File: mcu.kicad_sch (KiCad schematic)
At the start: 7 parts, among them U7 RP2040

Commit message: simulation
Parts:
- C12, C14, C15, C16, C17, C5: value C -> 10n; Part Number (none) -> -
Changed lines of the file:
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@@
 			)
 		)
-		(property "Value" "C"
+		(property "Value" "10n"
 			(at 166.37 30.4799 0)
 			(effects
@@
 				)
 				(hide yes)
+			)
+		)
+		(property "Part Number" "-"
+			(at 162.56 29.21 0)
+			(effects
+				(font
+					(size 1.27 1.27)
+				)
 			)
 		)
@@
 			)
 		)
+		(property "Part Number" ""
+			(at 127 81.28 0)
+			(effects
+				(font
+					(size 1.27 1.27)
+				)
+			)
+		)
 		(pin "55"
 		)
@@
 			)
 		)
-		(property "Value" "C"
+		(property "Value" "10n"
 			(at 106.68 30.4799 0)
 			(effects
@@
 				)
 				(hide yes)
+			)
+		)
+		(property "Part Number" "-"
+			(at 102.87 29.21 0)
+			(effects
+				(font
+					(size 1.27 1.27)
+				)
 			)
 		)
@@
 			)
 		)
-		(property "Value" "C"
+		(property "Value" "10n"
 			(at 146.05 30.4799 0)
 			(effects
@@
 				)
 				(hide yes)
+			)
+		)
+		(property "Part Number" "-"
+			(at 142.24 29.21 0)
+			(effects
+				(font
+					(size 1.27 1.27)
+				)
 			)
 		)
@@
 			)
 		)
-		(property "Value" "C"
+		(property "Value" "10n"
 			(at 116.84 30.4799 0)
 			(effects
@@
 				)
 				(hide yes)
+			)
+		)
+		(property "Part Number" "-"
+			(at 113.03 29.21 0)
+			(effects
+				(font
+					(size 1.27 1.27)
+				)
 			)
 		)
@@
 			)
 		)
-		(property "Value" "C"
+		(property "Value" "10n"
 			(at 156.21 30.4799 0)
 			(effects
@@
 				)
 				(hide yes)
+			)
+		)
+		(property "Part Number" "-"
+			(at 152.4 29.21 0)
+			(effects
+				(font
+					(size 1.27 1.27)
+				)
 			)
 		)
@@
 			)
 		)
-		(property "Value" "C"
+		(property "Value" "10n"
 			(at 96.52 30.4799 0)
 			(effects
@@
 			)
 		)
+		(property "Part Number" "-"
+			(at 92.71 29.21 0)
+			(effects
+				(font
+					(size 1.27 1.27)
+				)
+			)
+		)

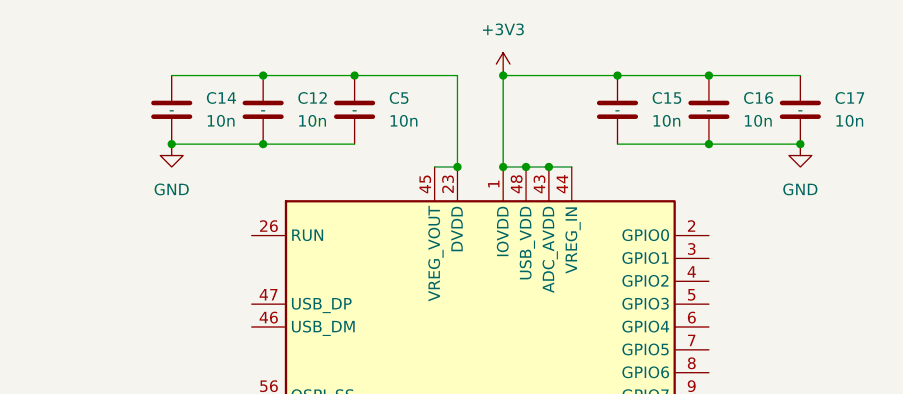
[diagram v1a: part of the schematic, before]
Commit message: new FET
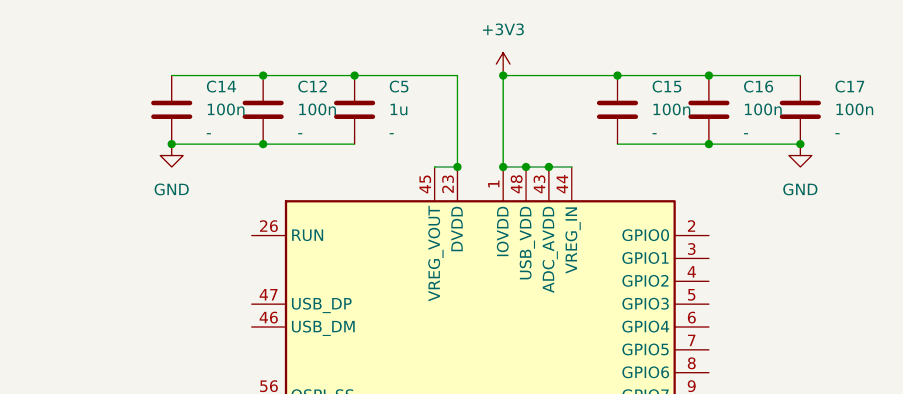
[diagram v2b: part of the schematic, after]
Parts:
- C12, C14, C15, C16, C17: value 10n -> 100n
- C5: value 10n -> 1u
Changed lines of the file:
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@@
 		(fields_autoplaced yes)
 		(property "Reference" "C17"
-			(at 166.37 27.9399 0)
-			(effects
-				(font
-					(size 1.27 1.27)
-				)
-				(justify left)
-			)
-		)
-		(property "Value" "10n"
-			(at 166.37 30.4799 0)
+			(at 166.37 26.6699 0)
+			(effects
+				(font
+					(size 1.27 1.27)
+				)
+				(justify left)
+			)
+		)
+		(property "Value" "100n"
+			(at 166.37 29.2099 0)
 			(effects
 				(font
@@
 		)
 		(property "Part Number" "-"
-			(at 162.56 29.21 0)
-			(effects
-				(font
-					(size 1.27 1.27)
-				)
+			(at 166.37 31.7499 0)
+			(effects
+				(font
+					(size 1.27 1.27)
+				)
+				(justify left)
 			)
 		)
@@
 		(fields_autoplaced yes)
 		(property "Reference" "C12"
-			(at 106.68 27.9399 0)
-			(effects
-				(font
-					(size 1.27 1.27)
-				)
-				(justify left)
-			)
-		)
-		(property "Value" "10n"
-			(at 106.68 30.4799 0)
+			(at 106.68 26.6699 0)
+			(effects
+				(font
+					(size 1.27 1.27)
+				)
+				(justify left)
+			)
+		)
+		(property "Value" "100n"
+			(at 106.68 29.2099 0)
 			(effects
 				(font
@@
 		)
 		(property "Part Number" "-"
-			(at 102.87 29.21 0)
-			(effects
-				(font
-					(size 1.27 1.27)
-				)
+			(at 106.68 31.7499 0)
+			(effects
+				(font
+					(size 1.27 1.27)
+				)
+				(justify left)
 			)
 		)
@@
 		(fields_autoplaced yes)
 		(property "Reference" "C15"
-			(at 146.05 27.9399 0)
-			(effects
-				(font
-					(size 1.27 1.27)
-				)
-				(justify left)
-			)
-		)
-		(property "Value" "10n"
-			(at 146.05 30.4799 0)
+			(at 146.05 26.6699 0)
+			(effects
+				(font
+					(size 1.27 1.27)
+				)
+				(justify left)
+			)
+		)
+		(property "Value" "100n"
+			(at 146.05 29.2099 0)
 			(effects
 				(font
@@
 		)
 		(property "Part Number" "-"
-			(at 142.24 29.21 0)
-			(effects
-				(font
-					(size 1.27 1.27)
-				)
+			(at 146.05 31.7499 0)
+			(effects
+				(font
+					(size 1.27 1.27)
+				)
+				(justify left)
 			)
 		)
@@
 		(fields_autoplaced yes)
 		(property "Reference" "C5"
-			(at 116.84 27.9399 0)
-			(effects
-				(font
-					(size 1.27 1.27)
-				)
-				(justify left)
-			)
-		)
-		(property "Value" "10n"
-			(at 116.84 30.4799 0)
+			(at 116.84 26.6699 0)
+			(effects
+				(font
+					(size 1.27 1.27)
+				)
+				(justify left)
+			)
+		)
+		(property "Value" "1u"
+			(at 116.84 29.2099 0)
 			(effects
 				(font
@@
 		)
 		(property "Part Number" "-"
-			(at 113.03 29.21 0)
-			(effects
-				(font
-					(size 1.27 1.27)
-				)
+			(at 116.84 31.7499 0)
+			(effects
+				(font
+					(size 1.27 1.27)
+				)
+				(justify left)
 			)
 		)
@@
 		(fields_autoplaced yes)
 		(property "Reference" "C16"
-			(at 156.21 27.9399 0)
-			(effects
-				(font
-					(size 1.27 1.27)
-				)
-				(justify left)
-			)
-		)
-		(property "Value" "10n"
-			(at 156.21 30.4799 0)
+			(at 156.21 26.6699 0)
+			(effects
+				(font
+					(size 1.27 1.27)
+				)
+				(justify left)
+			)
+		)
+		(property "Value" "100n"
+			(at 156.21 29.2099 0)
 			(effects
 				(font
@@
 		)
 		(property "Part Number" "-"
-			(at 152.4 29.21 0)
-			(effects
-				(font
-					(size 1.27 1.27)
-				)
+			(at 156.21 31.7499 0)
+			(effects
+				(font
+					(size 1.27 1.27)
+				)
+				(justify left)
 			)
 		)
@@
 		(fields_autoplaced yes)
 		(property "Reference" "C14"
-			(at 96.52 27.9399 0)
-			(effects
-				(font
-					(size 1.27 1.27)
-				)
-				(justify left)
-			)
-		)
-		(property "Value" "10n"
-			(at 96.52 30.4799 0)
+			(at 96.52 26.6699 0)
+			(effects
+				(font
+					(size 1.27 1.27)
+				)
+				(justify left)
+			)
+		)
+		(property "Value" "100n"
+			(at 96.52 29.2099 0)
 			(effects
 				(font
@@
 		)
 		(property "Part Number" "-"
-			(at 92.71 29.21 0)
-			(effects
-				(font
-					(size 1.27 1.27)
-				)
-			)
-		)
+			(at 96.52 31.7499 0)
+			(effects
+				(font
+					(size 1.27 1.27)
+				)
+				(justify left)
+			)
+		)

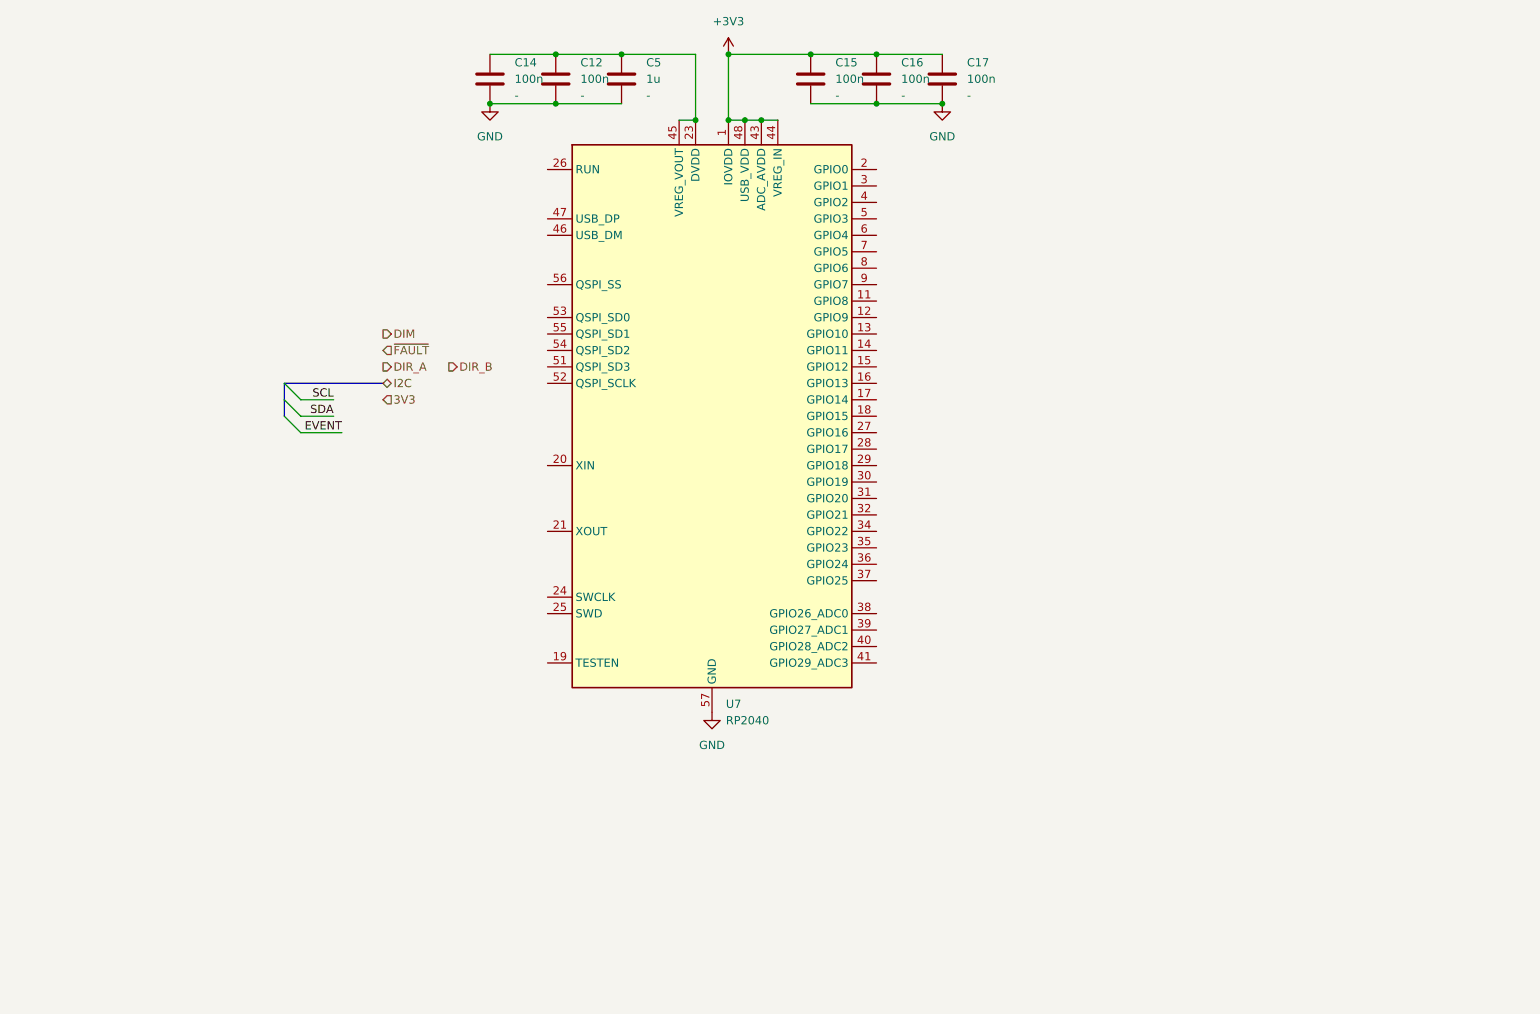
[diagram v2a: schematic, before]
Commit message: updated components
New ganfet selected and further work developing the rp2040 microcontroller circuit
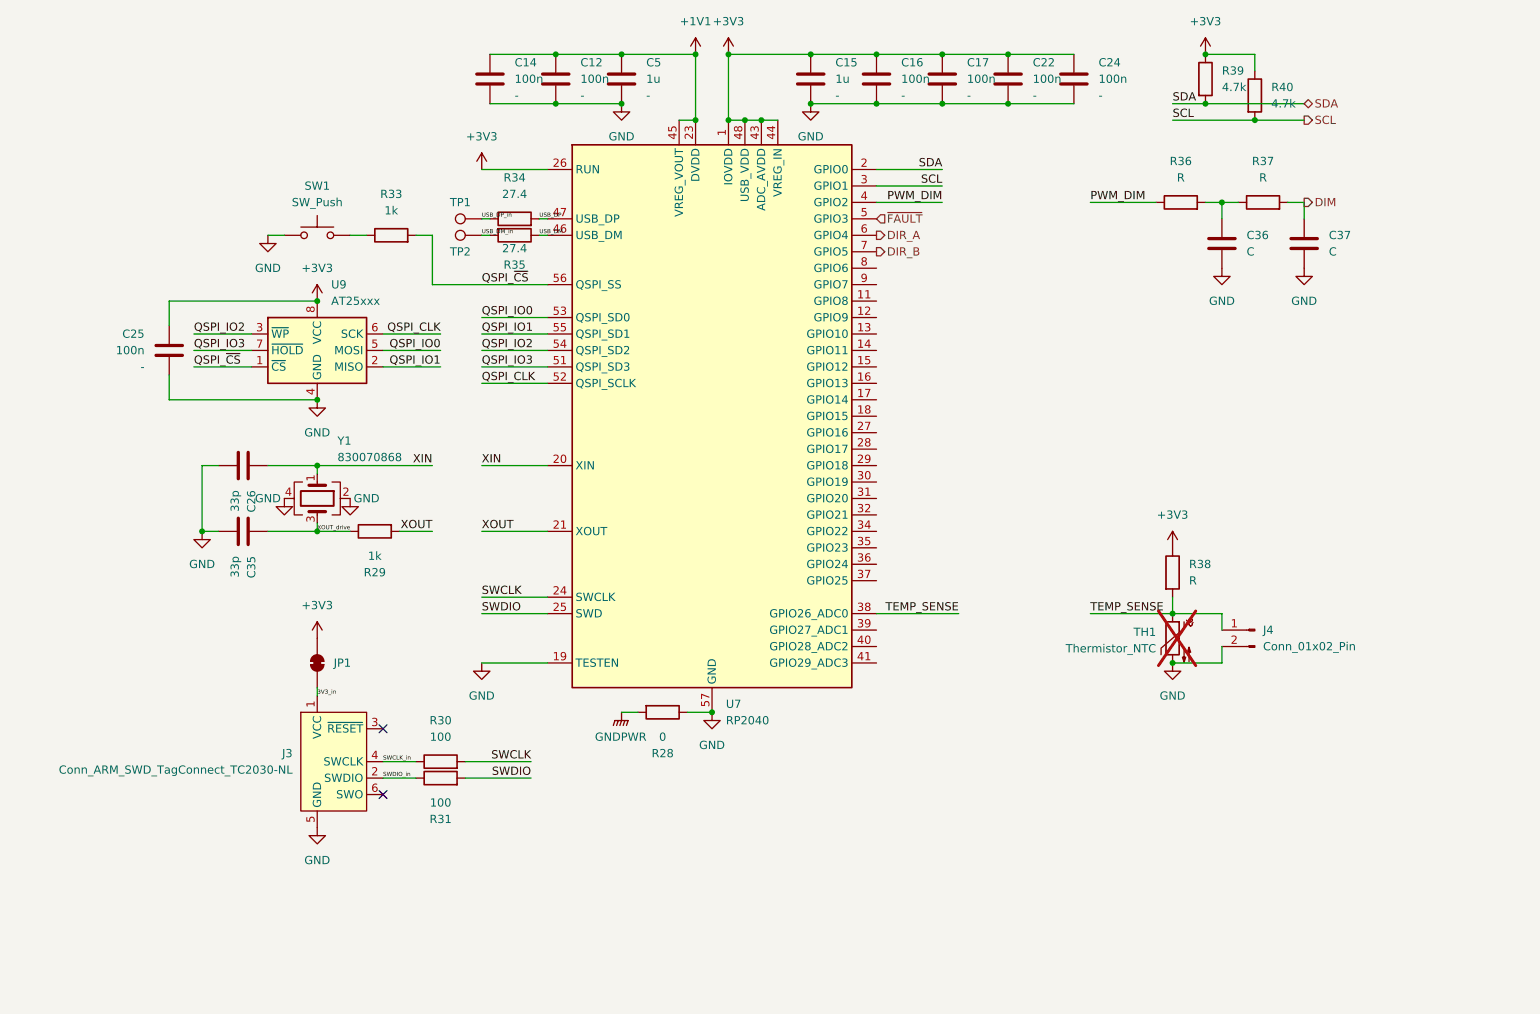
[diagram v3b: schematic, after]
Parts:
- added C22, C24, C25: 100n, Capacitor_SMD:C_0603_1608Metric, symbol Device:C
- added C26, C35: 33p, Capacitor_SMD:C_0603_1608Metric, symbol Device:C
- added C36, C37: C, Capacitor_SMD:C_0603_1608Metric, symbol Device:C
- added J3: Conn_ARM_SWD_TagConnect_TC2030-NL, Connector:Tag-Connect_TC2030-IDC-NL_2x03_P1.27mm_Vertical, symbol Connector:Conn_ARM_SWD_TagConnect_TC2030-NL
- added J4: Conn_01x02_Pin, Connector_PinHeader_2.54mm:PinHeader_1x02_P2.54mm_Vertical, symbol Connector:Conn_01x02_Pin
- added JP1: SolderJumper_2_Bridged, Jumper:SolderJumper-2_P1.3mm_Bridged2Bar_RoundedPad1.0x1.5mm, symbol Jumper:SolderJumper_2_Bridged
- added R28: 0, Resistor_SMD:R_0603_1608Metric, symbol Device:R
- added R29, R33: 1k, Resistor_SMD:R_0603_1608Metric, symbol Device:R
- added R30, R31: 100, Resistor_SMD:R_0603_1608Metric, symbol Device:R
- added R34, R35: 27.4, Resistor_SMD:R_0603_1608Metric, symbol Device:R
- added R36, R37, R38: R, Resistor_SMD:R_0603_1608Metric, symbol Device:R
- added R39, R40: 4.7k, Resistor_SMD:R_0603_1608Metric, symbol Device:R
- added SW1: SW_Push, symbol Switch:SW_Push
- added TH1: Thermistor_NTC, symbol Device:Thermistor_NTC
- added TP1, TP2: TestPoint, TestPoint:TestPoint_Pad_D2.0mm, symbol Connector:TestPoint
- added U9: AT25xxx, Package_SO:SOIC-8_3.9x4.9mm_P1.27mm, symbol Memory_EEPROM:AT25xxx
- added Y1: 830070868, Crystal:Crystal_SMD_3225-4Pin_3.2x2.5mm, symbol Device:Crystal_GND24
- C15: value 100n -> 1u
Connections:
- net +3V3: now also U7.26 (RUN), C22.1, C24.1, C25.1, JP1.2 (B), R38.1, R39.1, R40.1, U9.8 (VCC)
- net DIM: now also C37.1, R37.2
- net DIR_A: now also U7.6 (GPIO4)
- net DIR_B: now also U7.7 (GPIO5)
- net GND: now also U7.19 (TESTEN), C22.2, C24.2, C25.2, C26.2, C35.2, C36.2, C37.2, J3.5 (GND), J4.2 (Pin_2), R28.1, SW1.1, TH1.2, U9.4 (GND), Y1.2, Y1.4
- net SCL: now also U7.3 (GPIO1), R40.2
- net SDA: now also U7.2 (GPIO0), R39.2
- net ~{FAULT}: now also U7.5 (GPIO3)
- net XIN: now reaches U7.20 (XIN)
- net XIN: now also C26.1, Y1.1
- net XOUT: now reaches U7.21 (XOUT)
- net XOUT: now also R29.2
- net +1V1: now reaches C12.1, C14.1, C5.1, U7.23 (DVDD), U7.45 (VREG_VOUT), U7.50 (DVDD)
- net SWCLK: now reaches U7.24 (SWCLK)
- net SWCLK: now also R30.2
- net SWDIO: now reaches U7.25 (SWD)
- net SWDIO: now also R31.2
- net TEMP_SENSE: now reaches U7.38 (GPIO26_ADC0)
- net TEMP_SENSE: now also J4.1 (Pin_1), R38.2, TH1.1
- net PWM_DIM: now reaches U7.4 (GPIO2)
- net PWM_DIM: now also R36.1
- net USB_DM: now reaches U7.46 (USB_DM)
- net USB_DM: now also R35.1
- net USB_DP: now reaches U7.47 (USB_DP)
- net USB_DP: now also R34.2
- net QSPI_IO3: now reaches U7.51 (QSPI_SD3)
- net QSPI_IO3: now also U9.7 (~{HOLD})
- net QSPI_CLK: now reaches U7.52 (QSPI_SCLK)
- net QSPI_CLK: now also U9.6 (SCK)
- net QSPI_IO0: now reaches U7.53 (QSPI_SD0)
- net QSPI_IO0: now also U9.5 (MOSI)
- net QSPI_IO2: now reaches U7.54 (QSPI_SD2)
- net QSPI_IO2: now also U9.3 (~{WP})
- net QSPI_IO1: now reaches U7.55 (QSPI_SD1)
- net QSPI_IO1: now also U9.2 (MISO)
- net QSPI_~{CS}: now reaches U7.56 (QSPI_SS)
- net QSPI_~{CS}: now also R33.2, U9.1 (~{CS})
- new net: C36.1, R36.2, R37.1
- new net: R33.1, SW1.2
- new net 3V3_in: J3.1 (VCC), JP1.1 (A)
- new net GNDPWR: R28.2
- new net SWCLK_in: J3.4 (SWCLK), R30.1
- new net SWDIO_in: J3.2 (SWDIO), R31.1
- new net USB_DM_in: R35.2, TP2.1
- new net USB_DP_in: R34.1, TP1.1
- new net XOUT_drive: C35.1, R29.1, Y1.3
- no-connect marks 0 -> 2

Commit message: board routing progress
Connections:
- no-connect marks 2 -> 25
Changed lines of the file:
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@@
+	)
+	(no_connect
+		(at 152.4 58.42)
+	)
+	(no_connect
+		(at 152.4 73.66)
+	)
+	(no_connect
+		(at 152.4 81.28)
+	)
+	(no_connect
+		(at 152.4 68.58)
 	)
 	(no_connect
 		(at 76.2 129.54)
 	)
+	(no_connect
+		(at 152.4 76.2)
+	)
+	(no_connect
+		(at 152.4 101.6)
+	)
+	(no_connect
+		(at 152.4 86.36)
+	)
+	(no_connect
+		(at 152.4 91.44)
+	)
+	(no_connect
+		(at 152.4 66.04)
+	)
+	(no_connect
+		(at 152.4 106.68)
+	)
+	(no_connect
+		(at 152.4 88.9)
+	)
+	(no_connect
+		(at 152.4 96.52)
+	)
+	(no_connect
+		(at 152.4 63.5)
+	)
+	(no_connect
+		(at 152.4 93.98)
+	)
+	(no_connect
+		(at 152.4 119.38)
+	)
+	(no_connect
+		(at 152.4 78.74)
+	)
+	(no_connect
+		(at 152.4 114.3)
+	)
+	(no_connect
+		(at 152.4 104.14)
+	)
+	(no_connect
+		(at 152.4 99.06)
+	)
+	(no_connect
+		(at 152.4 83.82)
+	)
+	(no_connect
+		(at 152.4 60.96)
+	)
+	(no_connect
+		(at 152.4 116.84)
+	)
+	(no_connect
+		(at 152.4 71.12)
+	)
 	(wire

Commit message: full layout
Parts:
- removed C14: 100n, Capacitor_SMD:C_0603_1608Metric, symbol Device:C
- removed SW1: SW_Push, symbol Switch:SW_Push
- added S1: 435171014816, 435171014816:435171014816, symbol 435171014816:435171014816
- C15: Note (none) -> Place close to RP2040 pin 44
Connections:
- net GND: now also S1.3, S1.4, S1.5, S1.6
- net at R33.1: now also S1.1, S1.2
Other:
- moved on the sheet: R33

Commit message: finished board
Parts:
- removed JP1: SolderJumper_2_Bridged, Jumper:SolderJumper-2_P1.3mm_Bridged2Bar_RoundedPad1.0x1.5mm, symbol Jumper:SolderJumper_2_Bridged
- C15: Note Place close to RP2040 pin 44 -> Place 1uF close to RP2040 pin 44
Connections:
- net 3V3_in is gone; now on net +3V3: J3.1 (VCC)
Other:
- moved on the sheet: C12, C15, C16, C17, C22, C24, C25, C26, C35, C36, C37, C5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

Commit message: production design files
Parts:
- J3: now in the parts list
- J4, TP1, TP2: now left out of the parts list
- S1: Part Number (none) -> P19889CT-ND
- TH1: Part Number (none) -> 56-NTCLP450E3104H-ND
- U7: Part Number (none) -> 2648-SC0914(13)CT-ND
- U9: Part Number (none) -> 1265-AT25FF081A-SSHN-B-ND
- Y1: Part Number (none) -> 732-830070868CT-ND
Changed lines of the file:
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@@
 			)
 		)
-		(property "Datasheet" "~"
+		(property "Datasheet" "https://www.vishay.com/docs/29110/ntclp450e3.pdf"
 			(at 220.98 134.62 0)
 			(effects
@@
 			)
 		)
+		(property "Part Number" "56-NTCLP450E3104H-ND"
+			(at 220.98 135.89 0)
+			(effects
+				(font
+					(size 1.27 1.27)
+				)
+				(hide yes)
+			)
+		)
 		(pin "2"
 		)
@@
 				)
 				(justify left)
+				(hide yes)
 			)
 		)
@@
 		(unit 1)
 		(exclude_from_sim no)
-		(in_bom no)
+		(in_bom yes)
 		(on_board yes)
 		(dnp no)
@@
 			)
 		)
+		(property "Part Number" "1265-AT25FF081A-SSHN-B-ND"
+			(at 91.44 91.44 0)
+			(effects
+				(font
+					(size 1.27 1.27)
+				)
+				(hide yes)
+			)
+		)
 		(pin "4"
 		)
@@
 		(unit 1)
 		(exclude_from_sim no)
-		(in_bom yes)
+		(in_bom no)
 		(on_board yes)
 		(dnp no)
@@
 			)
 		)
-		(property "Part Number" ""
+		(property "Part Number" "2648-SC0914(13)CT-ND"
 			(at 152.4 101.6 0)
 			(effects
@@
 					(size 1.27 1.27)
 				)
+				(hide yes)
 			)
 		)
@@
 		(unit 1)
 		(exclude_from_sim no)
-		(in_bom yes)
+		(in_bom no)
 		(on_board yes)
 		(dnp no)
@@
 				)
 				(justify left)
+				(hide yes)
 			)
 		)
@@
 				)
 				(justify left)
+				(hide yes)
 			)
 		)
@@
 				)
 				(justify left)
+				(hide yes)
 			)
 		)
@@
 				)
 				(justify left)
+				(hide yes)
 			)
 		)
@@
 				)
 				(justify left)
+				(hide yes)
 			)
 		)
@@
 				)
 				(justify left)
+				(hide yes)
 			)
 		)
@@
 				)
 				(justify left)
+				(hide yes)
 			)
 		)
@@
 			)
 		)
+		(property "Part Number" "732-830070868CT-ND"
+			(at 91.44 114.3 0)
+			(effects
+				(font
+					(size 1.27 1.27)
+				)
+				(hide yes)
+			)
+		)
 		(pin "2"
 		)
@@
 			)
 		)
-		(property "Datasheet" ""
+		(property "Datasheet" "https://www3.panasonic.biz/ac/e_download/control/switch/light-touch/catalog/sw_lt_eng_2616s.pdf"
 			(at 91.44 63.5 0)
 			(effects
@@
 			)
 		)
+		(property "Part Number" "P19889CT-ND"
+			(at 91.44 63.5 0)
+			(effects
+				(font
+					(size 1.27 1.27)
+				)
+				(hide yes)
+			)
+		)
 		(pin "2"
 		)
@@
 		(unit 1)
 		(exclude_from_sim no)
-		(in_bom yes)
+		(in_bom no)
 		(on_board yes)
 		(dnp no)
